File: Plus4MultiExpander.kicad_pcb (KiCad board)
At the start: 2 copper layers, 62.2 x 99.9 mm, 11 parts, among them CN1 EDGE_CONN, CN2 C16_NEWSTYLE_EXP_PORT_1, CN3 C16_NEWSTYLE_EXP_PORT_2, CN4 C16_NEWSTYLE_EXP_PORT_3, U1 74LS245, U2 74LS245

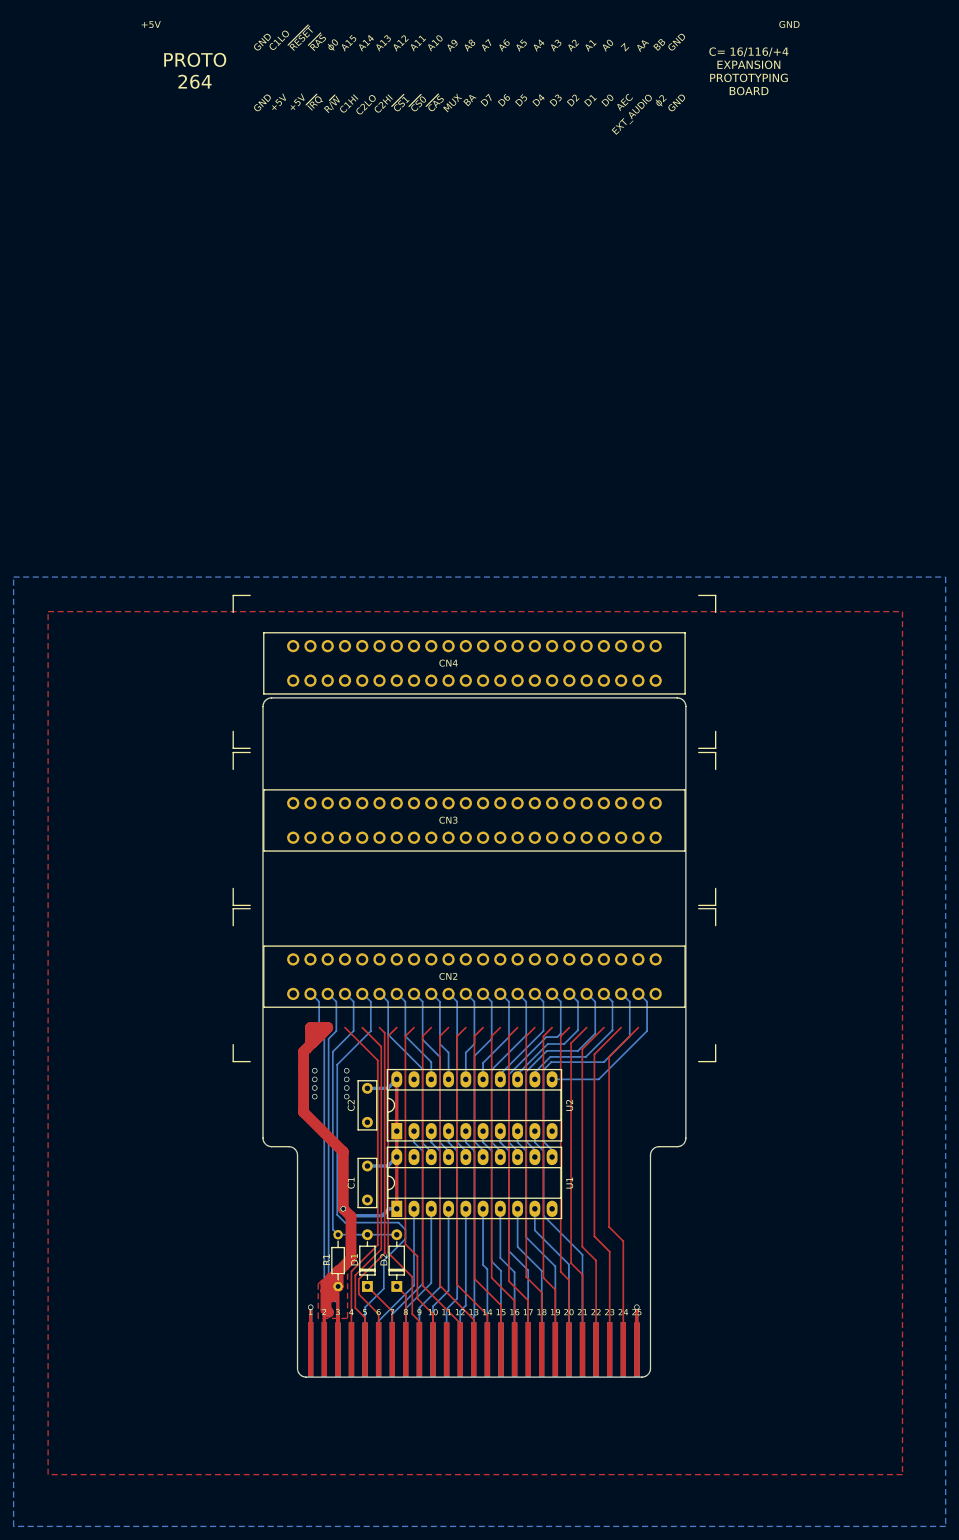
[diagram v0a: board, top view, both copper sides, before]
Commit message: Space connectors properly Needs cleanup but board is there
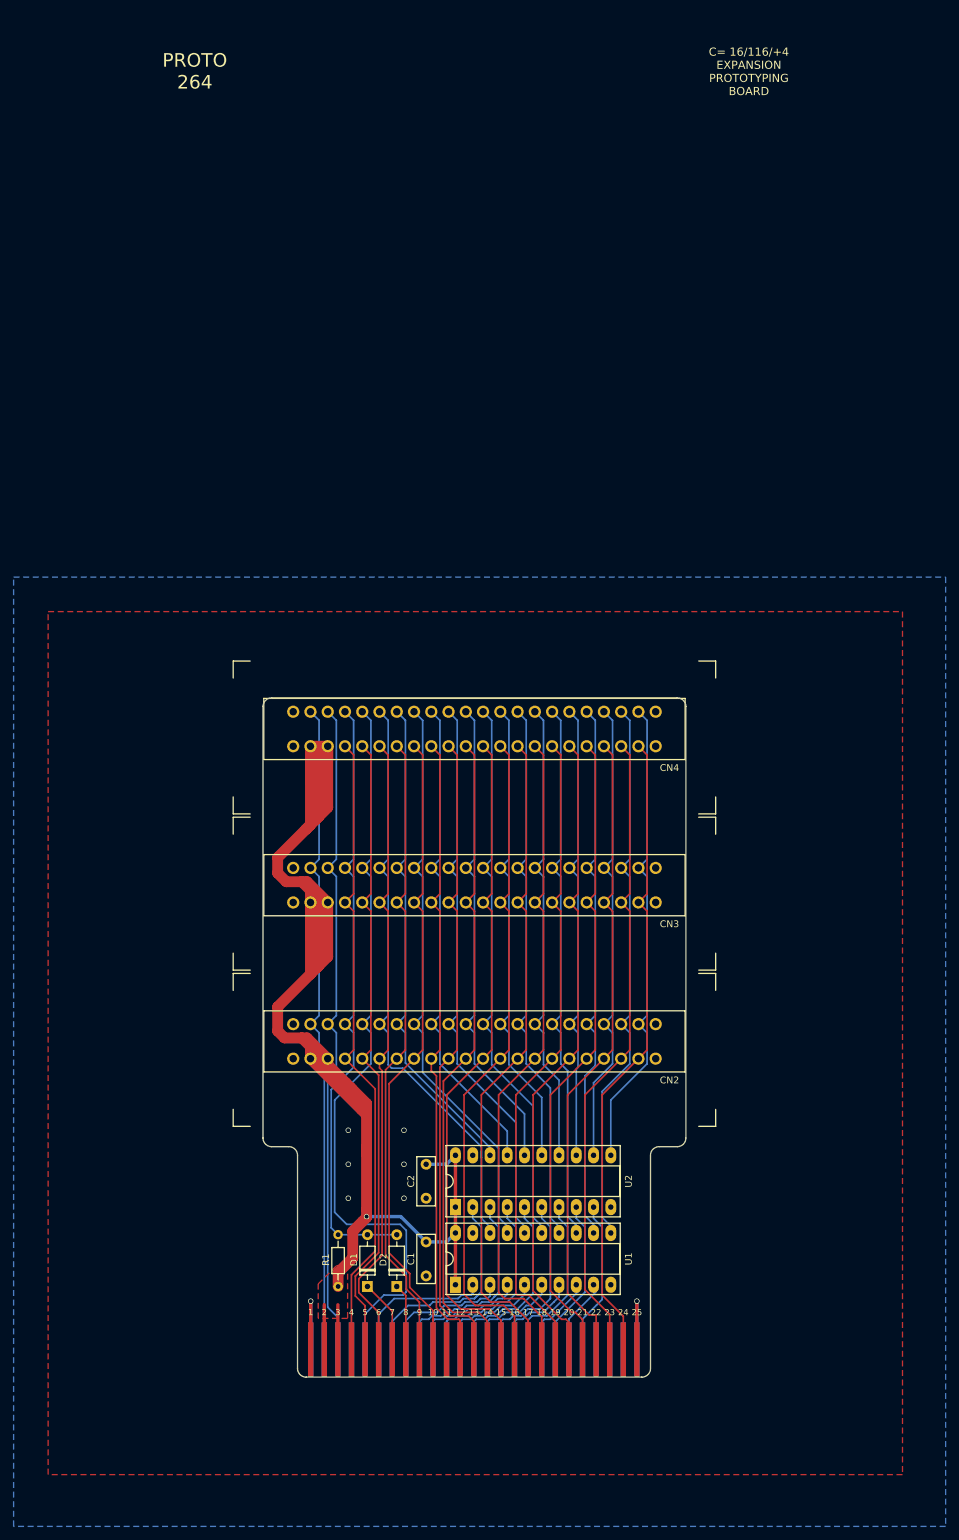
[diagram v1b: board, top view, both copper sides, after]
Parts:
- moved U1 14.1 mm to (149.5, 134.5)
- moved U2 14.1 mm to (149.5, 123.1)
- moved C1 14.1 mm to (145.2, 128.2)
- moved C2 14.1 mm to (145.2, 116.8)
- moved CN4 9.65 mm to (152.3, 52.7)
- moved CN2 9.53 mm to (152.3, 98.7)
- moved CN3 9.52 mm to (152.3, 75.7)
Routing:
- net +5V: track 119.1 -> 240.8 mm
- net /ba15: track 27.3 -> 87.5 mm
- net /ba11: track 25.2 -> 83.4 mm
- net /ba14: track 14.8 -> 73.1 mm
- net /ba12: track 13.8 -> 72.0 mm
- net /ba13: track 26.2 -> 84.5 mm
- net /ba10: track 13.8 -> 71.0 mm
- net /ba9: track 26.2 -> 82.4 mm
- net /ba8: track 14.8 -> 69.9 mm
- net /ba7: track 27.3 -> 81.3 mm
- net /ba6: track 15.9 -> 68.9 mm, vias 1 -> 0
- net /ba5: track 29.3 -> 80.3 mm
- net /ba4: track 18.3 -> 68.0 mm
- net /phi0: track 66.3 -> 115.9 mm
- net /d6: track 49.5 -> 98.9 mm
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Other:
- board text removed: "C2HI"
- board text removed: "~CAS"
- board text removed: "~RAS"

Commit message: Honing
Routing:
- net /a3: track 12.3 -> 13.4 mm
- net /a1: track 11.2 -> 12.0 mm
- net /aec: track 95.4 -> 94.8 mm
- net /phi0: track 115.9 -> 115.3 mm
- net /d3: track 97.4 -> 96.8 mm
- net /a15: track 21.6 -> 21.1 mm
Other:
- board text added: "C16/Plus4 MULTI EXPANDER"
- board text added: "~C1HI"
- board text added: "~C1LO"
- board text added: "~C2"
- board text removed: "C1HI"
- board text removed: "C1LO"
- board text removed: "C2LO"
- board text removed: "C= 16/116/+4 EXPANSION PROTOTYPING BOARD"
- board text removed: "PROTO 264"
